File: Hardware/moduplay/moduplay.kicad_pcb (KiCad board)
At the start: 2 copper layers, 72 x 60 mm, 14 parts, among them SW1 Left, SW10 Power_Switch, SW2 Up, SW3 Right, SW4 Down, SW5 X, SW6 Y, SW7 B, SW8 A, SW9 Menu

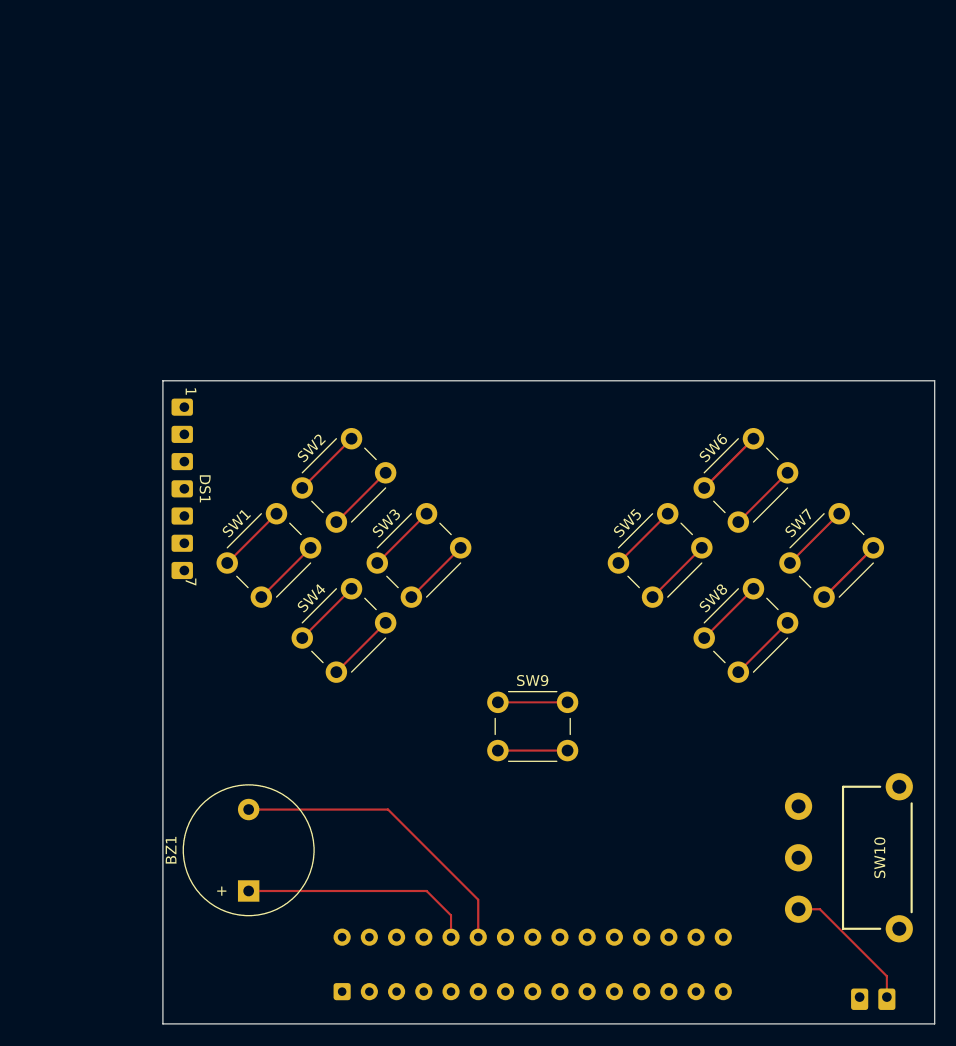
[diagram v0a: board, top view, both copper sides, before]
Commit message: Add buzzer switch, separete baterry connectors, further PCD development
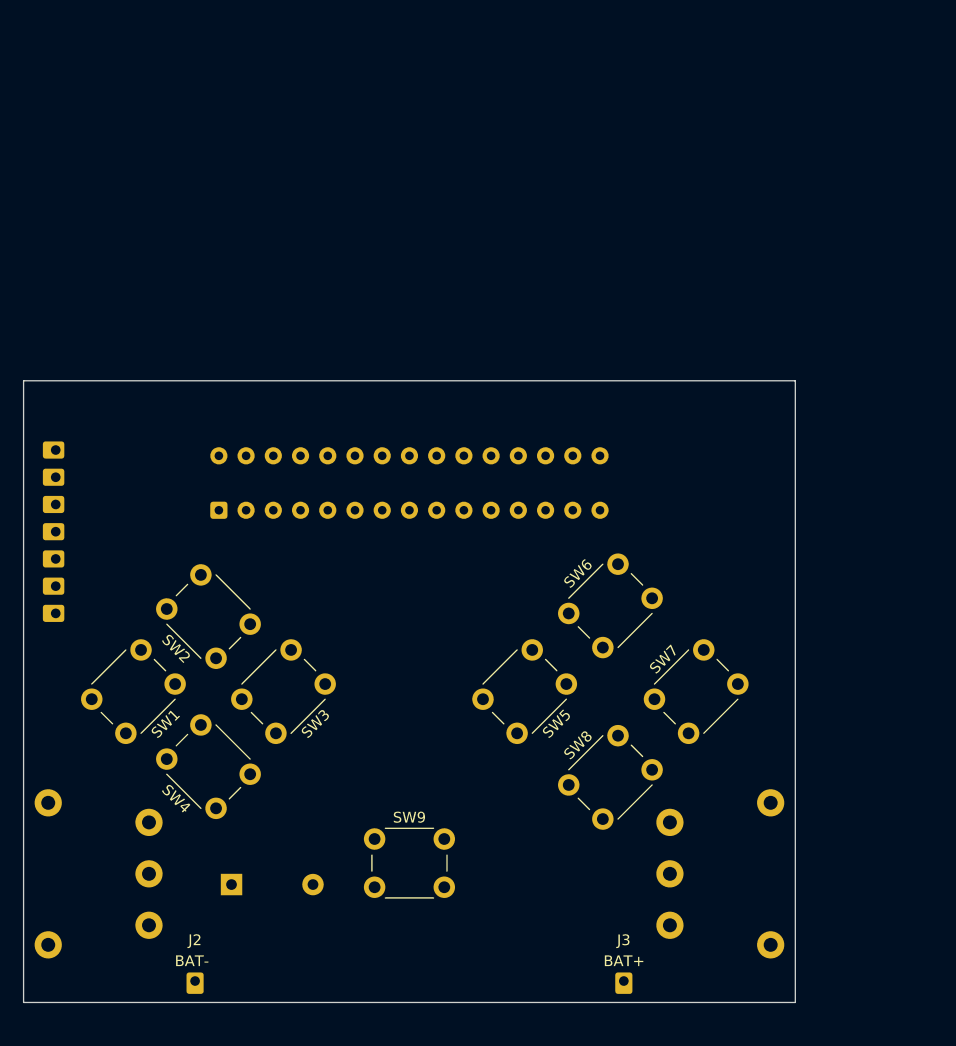
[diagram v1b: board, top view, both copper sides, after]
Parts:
- removed BT1: Battery, local:Power_Port
- added J2: -, local:Power_Port_Single_Minus, F.Cu at (130.0, 116.0)
- added J3: +, local:Power_Port_Single_Plus, F.Cu at (170.0, 116.0)
- added SW11: Buzzer_Switch, local:Power_Switch, B.Cu at (125.7, 106.0)
- BZ1, DS1, SW10: moved to B.Cu
- moved J1 46.4 mm to (150.0, 67.0)
- moved SW9 17.1 mm to (150.0, 105.0)
- moved SW8 15.7 mm to (168.8, 97.0)
- moved SW1 14.9 mm to (124.2, 89.0), turned to -135 degrees
- moved SW2 14.9 mm to (131.2, 82.0), turned to 135 degrees
- moved SW3 14.9 mm to (138.2, 89.0), turned to -135 degrees
- moved SW4 14.9 mm to (131.2, 96.0), turned to 135 degrees
- moved SW5 14.9 mm to (160.8, 89.0), turned to -135 degrees
- moved SW7 14.9 mm to (176.8, 89.0)
- moved SW6 14.1 mm to (168.8, 81.0)
- moved DS1 12.6 mm to (117.0, 74.1), turned to 90 degrees
- moved SW10 12.1 mm to (174.3, 106.0), turned to -90 degrees
- moved BZ1 1.71 mm to (133.4, 107.0), turned to 0 degrees
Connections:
- J1 pad 10: Net-(BZ1-+) -> Net-(J1-BUZZ1)
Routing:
- net Net-(BZ1--): track 28.4 -> 0.00 mm
- net Net-(BZ1-+): track 21.9 -> 0.00 mm
- net Net-(J3-Pin_1): track 12.8 -> 0.00 mm
- net Net-(J1-BTN_Y2): track 6.50 -> 0.00 mm
- net Net-(J1-BTN_X1): track 6.50 -> 0.00 mm
- net Net-(J1-BTN_UP2): track 6.50 -> 0.00 mm
- net Net-(J1-BTN_RIGHT1): track 6.50 -> 0.00 mm
- net Net-(J1-BTN_LEFT1): track 6.50 -> 0.00 mm
- net Net-(J1-BTN_DOWN2): track 6.50 -> 0.00 mm
- net Net-(J1-BTN_B2): track 6.50 -> 0.00 mm
- net Net-(J1-BTN_A1): track 6.50 -> 0.00 mm
- net Net-(J1-BTN_MENU2): track 6.50 -> 0.00 mm
- net Net-(J1-BTN_MENU1): track 6.50 -> 0.00 mm
- net Net-(J1-BTN_Y1): track 6.50 -> 0.00 mm
- net Net-(J1-BTN_X2): track 6.50 -> 0.00 mm
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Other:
- board size 72 x 60 mm -> 72 x 58 mm

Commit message: Next iteration designing PCB
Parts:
- added REF**: OSHW-Logo2_9.8x8mm_SilkScreen, Symbol:OSHW-Logo2_9.8x8mm_SilkScreen, F.Cu at (180.0, 74.0)
- added REF**: KiCad-Logo2_5mm_SilkScreen, Symbol:KiCad-Logo2_5mm_SilkScreen, F.Cu at (178.0, 65.0)
- DS1: value ~ -> Display
- SW10: value Power_Switch -> Power
- SW11: value Buzzer_Switch -> Buzzer
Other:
- board text added: "1"
- board text added: "ModuPlay v0.1"

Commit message: Try to include whole screen
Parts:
- DS1: footprint local:Screen_Port -> local:Screen_Full; moved to F.Cu
- moved REF** 27.0 mm to (177.0, 38.0)
- moved REF** 26.1 mm to (178.0, 48.0)
- moved DS1 21.1 mm to (116.4, 53.0), turned to 0 degrees
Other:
- board size 72 x 58 mm -> 72 x 87 mm
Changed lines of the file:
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@@
 	(footprint "Symbol:OSHW-Logo2_9.8x8mm_SilkScreen"
 		(layer "F.Cu")
-		(at 180 74)
+		(at 178 48)
 		(descr "Open Source Hardware Symbol")
 		(tags "Logo Symbol OSHW")
@@
 		)
 	)
+	(footprint "local:Screen_Full"
+		(layer "F.Cu")
+		(at 116.42 53)
+		(property "Reference" "DS1"
+			(at 33.58 0 0)
+			(unlocked yes)
+			(layer "F.SilkS")
+			(effects
+				(font
+					(size 1 1)
+					(thickness 0.1)
+				)
+			)
+		)
+		(property "Value" "Display"
+			(at 33.655 -5.715 0)
+			(unlocked yes)
+			(layer "F.Fab")
+			(effects
+				(font
+					(size 1 1)
+					(thickness 0.15)
+				)
+			)
+		)
+		(property "Datasheet" ""
+			(at 0 0 0)
+			(unlocked yes)
+			(layer "F.Fab")
+			(hide yes)
+			(effects
+				(font
+					(size 1 1)
+					(thickness 0.15)
+				)
+			)
+		)
+		(property "Description" ""
+			(at 0 0 0)
+			(unlocked yes)
+			(layer "F.Fab")
+			(hide yes)
+			(effects
+				(font
+					(size 1 1)
+					(thickness 0.15)
+				)
+			)
+		)
+		(sheetname "/")
+		(sheetfile "moduplay.kicad_sch")
+		(attr through_hole)
+		(fp_poly
+			(pts
+				(xy -2.52 -21.575) (xy -2.52 21.575) (xy 69.68 21.575) (xy 69.68 -21.575)
+			)
+			(stroke
+				(width 0.2)
+				(type solid)
+			)
+			(fill no)
+			(layer "F.SilkS")
+		)
+		(fp_text user "7"
+			(at 1.905 -7.62 0)
+			(unlocked yes)
+			(layer "F.SilkS")
+			(effects
+				(font
+					(size 1 1)
+					(thickness 0.1)
+				)
+			)
+		)
+		(fp_text user "1"
+			(at 1.905 7.62 0)
+			(unlocked yes)
+			(layer "F.SilkS")
+			(effects
+				(font
+					(size 1 1)
+					(thickness 0.1)
+				)
+			)
+		)
+		(fp_text user "${REFERENCE}"
+			(at 33.02 6.985 0)
+			(unlocked yes)
+			(layer "F.Fab")
+			(effects
+				(font
+					(size 1 1)
+					(thickness 0.15)
+				)
+			)
+		)
+		(pad "1" thru_hole circle
+			(at 0 7.62 180)
+			(size 1.8 1.8)
+			(drill 0.9)
+			(layers "*.Cu" "*.Mask")
+			(remove_unused_layers no)
+			(net 1 "GND")
+			(pinfunction "VSS")
+			(pintype "power_in")
+		)
+		(pad "2" thru_hole circle
+			(at 0 5.079999 180)
+			(size 1.8 1.8)
+			(drill 0.9)
+			(layers "*.Cu" "*.Mask")
+			(remove_unused_layers no)
+			(net 9 "VCC")
+			(pinfunction "VDD")
+			(pintype "power_in")
+		)
+		(pad "3" thru_hole circle
+			(at 0 2.54 180)
+			(size 1.8 1.8)
+			(drill 0.9)
+			(layers "*.Cu" "*.Mask")
+			(remove_unused_layers no)
+			(net 7 "Net-(DS1-SCLK)")
+			(pinfunction "SCLK")
+			(pintype "input")
+		)
+		(pad "4" thru_hole circle
+			(at 0 0 180)
+			(size 1.8 1.8)
+			(drill 0.9)
+			(layers "*.Cu" "*.Mask")
+			(remove_unused_layers no)
+			(net 6 "Net-(DS1-SDA)")
+			(pinfunction "SDA")
+			(pintype "bidirectional")
+		)
+		(pad "5" thru_hole circle
+			(at 0 -2.54 180)
+			(size 1.8 1.8)
+			(drill 0.9)
+			(layers "*.Cu" "*.Mask")
+			(remove_unused_layers no)
+			(net 5 "Net-(DS1-RES)")
+			(pinfunction "RES")
+			(pintype "output")
+		)
+		(pad "6" thru_hole circle
+			(at 0 -5.079999 180)
+			(size 1.8 1.8)
+			(drill 0.9)
+			(layers "*.Cu" "*.Mask")
+			(remove_unused_layers no)
+			(net 8 "Net-(DS1-DC)")
+			(pinfunction "DC")
+			(pintype "input")
+		)
+		(pad "7" thru_hole circle
+			(at 0 -7.62 180)
+			(size 1.8 1.8)
+			(drill 0.9)
+			(layers "*.Cu" "*.Mask")
+			(remove_unused_layers no)
+			(net 4 "Net-(DS1-CS)")
+			(pinfunction "CS")
+			(pintype "input")
+		)
+		(embedded_fonts no)
+	)
 	(footprint "local:Power_Port_Single_Minus"
 		(layer "F.Cu")
@@
 	(footprint "Symbol:KiCad-Logo2_5mm_SilkScreen"
 		(layer "F.Cu")
-		(at 178 65)
+		(at 177 38)
 		(descr "KiCad Logo")
 		(tags "Logo KiCad")
@@
 		(embedded_fonts no)
 	)
-	(footprint "local:Screen_Port"
-		(layer "B.Cu")
-		(at 117 74.08 90)
-		(property "Reference" "DS1"
-			(at 0 1.905 270)
-			(unlocked yes)
-			(layer "B.SilkS")
-			(hide yes)
-			(effects
-				(font
-					(size 1 1)
-					(thickness 0.1)
-				)
-				(justify mirror)
-			)
-		)
-		(property "Value" "Display"
-			(at 0 2 270)
-			(unlocked yes)
-			(layer "B.SilkS")
-			(effects
-				(font
-					(size 1 1)
-					(thickness 0.15)
-				)
-				(justify mirror)
-			)
-		)
-		(property "Datasheet" ""
-			(at 0 0 270)
-			(unlocked yes)
-			(layer "B.Fab")
-			(hide yes)
-			(effects
-				(font
-					(size 1 1)
-					(thickness 0.15)
-				)
-				(justify mirror)
-			)
-		)
-		(property "Description" ""
-			(at 0 0 270)
-			(unlocked yes)
-			(layer "B.Fab")
-			(hide yes)
-			(effects
-				(font
-					(size 1 1)
-					(thickness 0.15)
-				)
-				(justify mirror)
-			)
-		)
-		(sheetname "/")
-		(sheetfile "moduplay.kicad_sch")
-		(attr through_hole)
-		(fp_text user "7"
-			(at 8.255 0 270)
-			(unlocked yes)
-			(layer "B.SilkS")
-			(effects
-				(font
-					(size 1 1)
-					(thickness 0.1)
-				)
-				(justify left bottom mirror)
-			)
-		)
-		(fp_text user "1"
-			(at -9.525 0 270)
-			(unlocked yes)
-			(layer "B.SilkS")
-			(effects
-				(font
-					(size 1 1)
-					(thickness 0.1)
-				)
-				(justify left bottom mirror)
-			)
-		)
-		(fp_text user "${REFERENCE}"
-			(at 0 -2.5 270)
-			(unlocked yes)
-			(layer "B.Fab")
-			(effects
-				(font
-					(size 1 1)
-					(thickness 0.15)
-				)
-				(justify mirror)
-			)
-		)
-		(pad "1" thru_hole roundrect
-			(at -7.62 0)
-			(size 2 1.6)
-			(drill 0.9
-				(offset -0.2 0)
-			)
-			(layers "*.Cu" "*.Mask")
-			(remove_unused_layers no)
-			(roundrect_rratio 0.15)
-			(net 1 "GND")
-			(pinfunction "VSS")
-			(pintype "power_in")
-			(thermal_bridge_angle 45)
-		)
-		(pad "2" thru_hole roundrect
-			(at -5.08 0)
-			(size 2 1.6)
-			(drill 0.9
-				(offset -0.2 0)
-			)
-			(layers "*.Cu" "*.Mask")
-			(remove_unused_layers no)
-			(roundrect_rratio 0.15)
-			(net 9 "VCC")
-			(pinfunction "VDD")
-			(pintype "power_in")
-			(thermal_bridge_angle 45)
-		)
-		(pad "3" thru_hole roundrect
-			(at -2.54 0)
-			(size 2 1.6)
-			(drill 0.9
-				(offset -0.2 0)
-			)
-			(layers "*.Cu" "*.Mask")
-			(remove_unused_layers no)
-			(roundrect_rratio 0.15)
-			(net 7 "Net-(DS1-SCLK)")
-			(pinfunction "SCLK")
-			(pintype "input")
-			(thermal_bridge_angle 45)
-		)
-		(pad "4" thru_hole roundrect
-			(at 0 0)
-			(size 2 1.6)
-			(drill 0.9
-				(offset -0.2 0)
-			)
-			(layers "*.Cu" "*.Mask")
-			(remove_unused_layers no)
-			(roundrect_rratio 0.15)
-			(net 6 "Net-(DS1-SDA)")
-			(pinfunction "SDA")
-			(pintype "bidirectional")
-			(thermal_bridge_angle 45)
-		)
-		(pad "5" thru_hole roundrect
-			(at 2.54 0)
-			(size 2 1.6)
-			(drill 0.9
-				(offset -0.2 0)
-			)
-			(layers "*.Cu" "*.Mask")
-			(remove_unused_layers no)
-			(roundrect_rratio 0.15)
-			(net 5 "Net-(DS1-RES)")
-			(pinfunction "RES")
-			(pintype "output")
-			(thermal_bridge_angle 45)
-		)
-		(pad "6" thru_hole roundrect
-			(at 5.08 0)
-			(size 2 1.6)
-			(drill 0.9
-				(offset -0.2 0)
-			)
-			(layers "*.Cu" "*.Mask")
-			(remove_unused_layers no)
-			(roundrect_rratio 0.15)
-			(net 8 "Net-(DS1-DC)")
-			(pinfunction "DC")
-			(pintype "input")
-			(thermal_bridge_angle 45)
-		)
-		(pad "7" thru_hole roundrect
-			(at 7.62 0)
-			(size 2 1.6)
-			(drill 0.9
-				(offset -0.2 0)
-			)
-			(layers "*.Cu" "*.Mask")
-			(remove_unused_layers no)
-			(roundrect_rratio 0.15)
-			(net 4 "Net-(DS1-CS)")
-			(pinfunction "CS")
-			(pintype "input")
-			(thermal_bridge_angle 45)
-		)
-		(embedded_fonts no)
-	)
 	(footprint "local:Edge_Connector_Slot"
 		(layer "B.Cu")
@@
 	)
 	(gr_rect
-		(start 114 118)
-		(end 186 60)
+		(start 114 31)
+		(end 186 118)
 		(stroke
 			(width 0.05)

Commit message: Improve screen position
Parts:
- moved REF** 5.50 mm to (178.0, 42.5)
- moved REF** 5.02 mm to (177.5, 33.0)
- moved DS1 5.00 mm to (116.4, 48.0)
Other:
- board size 72 x 87 mm -> 72.2 x 91.5 mm
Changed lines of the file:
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@@
 	(footprint "Symbol:OSHW-Logo2_9.8x8mm_SilkScreen"
 		(layer "F.Cu")
-		(at 178 48)
+		(at 178 42.5)
 		(descr "Open Source Hardware Symbol")
 		(tags "Logo Symbol OSHW")
@@
 	(footprint "local:Screen_Full"
 		(layer "F.Cu")
-		(at 116.42 53)
+		(at 116.42 48)
 		(property "Reference" "DS1"
 			(at 33.58 0 0)
 			(unlocked yes)
 			(layer "F.SilkS")
+			(hide yes)
 			(effects
 				(font
@@
 		(sheetfile "moduplay.kicad_sch")
 		(attr through_hole)
-		(fp_poly
-			(pts
-				(xy -2.52 -21.575) (xy -2.52 21.575) (xy 69.68 21.575) (xy 69.68 -21.575)
-			)
+		(fp_rect
+			(start -2.52 -21.575)
+			(end 69.68 21.575)
 			(stroke
-				(width 0.2)
+				(width 0.1)
 				(type solid)
 			)
 			(fill no)
-			(layer "F.SilkS")
+			(layer "Margin")
 		)
 		(fp_text user "7"
@@
 			)
 		)
-		(pad "1" thru_hole circle
+		(pad "1" thru_hole roundrect
 			(at 0 7.62 180)
 			(size 1.8 1.8)
@@
 			(layers "*.Cu" "*.Mask")
 			(remove_unused_layers no)
+			(roundrect_rratio 0.1388888889)
 			(net 1 "GND")
 			(pinfunction "VSS")
@@
 		)
 		(pad "2" thru_hole circle
-			(at 0 5.079999 180)
+			(at 0 5.08 180)
 			(size 1.8 1.8)
 			(drill 0.9)
@@
 		)
 		(pad "6" thru_hole circle
-			(at 0 -5.079999 180)
+			(at 0 -5.08 180)
 			(size 1.8 1.8)
 			(drill 0.9)
@@
 	(footprint "Symbol:KiCad-Logo2_5mm_SilkScreen"
 		(layer "F.Cu")
-		(at 177 38)
+		(at 177.5 33)
 		(descr "KiCad Logo")
 		(tags "Logo KiCad")
@@
 	)
 	(gr_rect
-		(start 114 31)
-		(end 186 118)
+		(start 113.9 118)
+		(end 186.1 26.5)
 		(stroke
 			(width 0.05)

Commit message: First draft of routing
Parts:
- removed REF**: OSHW-Logo2_9.8x8mm_SilkScreen, Symbol:OSHW-Logo2_9.8x8mm_SilkScreen
- removed REF**: KiCad-Logo2_5mm_SilkScreen, Symbol:KiCad-Logo2_5mm_SilkScreen
- turned SW3 to 45 degrees
- turned SW5 to 45 degrees
- turned SW8 to -135 degrees
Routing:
- net VCC: track 0.00 -> 129.8 mm, vias 0 -> 1
- net Net-(BZ1--): track 0.00 -> 100.0 mm
- net GND: track 0.00 -> 91.3 mm, vias 0 -> 1
- net Net-(J1-BTN_B2): track 0.00 -> 89.4 mm, vias 0 -> 1
- net Net-(J1-BUZZ1): track 0.00 -> 83.6 mm
- net Net-(J1-BTN_Y2): track 0.00 -> 79.9 mm, vias 0 -> 1
- net Net-(DS1-SDA): track 0.00 -> 78.9 mm, vias 0 -> 1
- net Net-(J1-BTN_B1): track 0.00 -> 77.8 mm, vias 0 -> 1
- net Net-(J1-BTN_DOWN1): track 0.00 -> 76.4 mm
- net Net-(J1-BTN_Y1): track 0.00 -> 71.2 mm, vias 0 -> 1
- net Net-(J1-BTN_DOWN2): track 0.00 -> 69.2 mm
- net Net-(J1-BTN_RIGHT1): track 0.00 -> 65.9 mm
- net Net-(DS1-CS): track 0.00 -> 65.0 mm
- net Net-(DS1-SCLK): track 0.00 -> 61.1 mm, vias 0 -> 1
- net Net-(DS1-RES): track 0.00 -> 58.3 mm
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
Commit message: Next iteration on PCB
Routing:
- net Net-(J1-BTN_Y1): track 71.2 -> 67.7 mm
- net Net-(J1-BTN_MENU1): track 47.1 -> 49.3 mm
- net Net-(J1-BTN_RIGHT2): track 52.8 -> 54.7 mm
- net Net-(J1-BTN_Y2): track 79.9 -> 78.0 mm
- net Net-(J1-BTN_B1): track 77.8 -> 79.1 mm
- net Net-(J3-Pin_1): track 6.98 -> 8.21 mm
- net Net-(J1-BTN_LEFT1): track 34.4 -> 35.4 mm
- net Net-(J1-BTN_B2): track 89.4 -> 90.1 mm
- net Net-(J1-BTN_RIGHT1): track 65.9 -> 66.6 mm
- net Net-(J1-BTN_UP1): track 34.5 -> 35.1 mm

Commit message: Final draft of PCB design
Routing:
- net VCC: track 129.8 -> 140.2 mm
- net Net-(DS1-SDA): track 78.9 -> 84.3 mm
- net Net-(DS1-CS): track 65.0 -> 67.9 mm
- net Net-(J1-BTN_X2): track 40.9 -> 43.7 mm
- net Net-(J1-BTN_X1): track 42.4 -> 44.9 mm
- net Net-(DS1-RES): track 58.3 -> 60.6 mm
- net Net-(J1-BTN_RIGHT2): track 54.7 -> 53.0 mm
- net Net-(J1-BTN_MENU2): track 42.1 -> 40.6 mm
- net Net-(BZ1--): track 100.0 -> 101.3 mm
- net Net-(DS1-SCLK): track 61.1 -> 62.2 mm
- net Net-(J1-BTN_A1): track 44.3 -> 43.5 mm
- net Net-(J1-BTN_RIGHT1): track 66.6 -> 67.4 mm
- net Net-(J1-BTN_A2): track 51.2 -> 50.4 mm
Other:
- board text added: "ModuPlay mk1"
- board text removed: "ModuPlay v0.1"
